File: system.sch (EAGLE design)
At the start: 36 parts, among them IC1 TPS7B8650BQDDARQ1, IC2 TLV9101IDBVR, IC3 TLV9101IDBVR, J1 TSW-104-07-F-S, J2 163-179PH-EX, U1 ATMEGA328PB-AU

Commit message: Added 0 ohm R for V_BG
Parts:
- added J3: RS1-02-G, RS1-02-G:RS1-02-G
- added R22, R23: 0, rcl:R-US_R0603
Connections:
- new net N$11: J3.2, R23.1
- net 0: now also J3.1
- net N$7: now also R22.1
- net V_BG: now also R22.2, R23.2
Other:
- note added: "AD2 Backup BG Voltage"
- note removed: "TODO: Add proper footprint for inductor R_L smol"
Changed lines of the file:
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@@
 <part name="R15" library="rcl" library_urn="urn:adsk.eagle:library:334" deviceset="R-US_" device="R0603" package3d_urn="urn:adsk.eagle:package:23555/3" value="0"/>
 <part name="R16" library="rcl" library_urn="urn:adsk.eagle:library:334" deviceset="R-US_" device="R0603" package3d_urn="urn:adsk.eagle:package:23555/3" value="0"/>
+<part name="R22" library="rcl" library_urn="urn:adsk.eagle:library:334" deviceset="R-US_" device="R0603" package3d_urn="urn:adsk.eagle:package:23555/3" value="0"/>
+<part name="J3" library="RS1-02-G" deviceset="RS1-02-G" device=""/>
+<part name="X_18" library="ngspice-simulation" library_urn="urn:adsk.eagle:library:527439" deviceset="GND" device=""/>
+<part name="R23" library="rcl" library_urn="urn:adsk.eagle:library:334" deviceset="R-US_" device="R0603" package3d_urn="urn:adsk.eagle:package:23555/3" value="0"/>
 </parts>
 <sheets>
@@
 <text x="-299.72" y="-71.12" size="1.778" layer="91">Decoupling cap</text>
 <text x="-154.94" y="-111.76" size="1.778" layer="91">Decoupling cap</text>
-<text x="-109.22" y="-127" size="1.778" layer="91">TODO:
-Add proper footprint for inductor
-R_L smol </text>
 <text x="-45.72" y="160.02" size="1.778" layer="91">Level Shifter
 Resistive divider with voltage follower
@@
 <text x="-39.37" y="-64.262" size="1.778" layer="91">Output</text>
 <text x="78.74" y="-83.82" size="1.778" layer="91">RST_ADC and V_TOGGLE from MCU</text>
+<text x="-200.66" y="30.48" size="1.778" layer="91">AD2 Backup BG Voltage</text>
 </plain>
 <moduleinsts>
@@
 <attribute name="NAME" value="LDO_AND_VOLTAGE_REFS" x="-119.38" y="63.5" size="2.032" layer="95" align="bottom-center"/>
 </moduleinst>
-<moduleinst name="BANDGAP_REF" module="BANDGAP_REF" x="-203.2" y="63.5">
-<attribute name="NAME" value="BANDGAP_REF" x="-203.2" y="63.5" size="2.032" layer="95" align="bottom-center"/>
+<moduleinst name="BANDGAP_REF" module="BANDGAP_REF" x="-210.82" y="63.5">
+<attribute name="NAME" value="BANDGAP_REF" x="-210.82" y="63.5" size="2.032" layer="95" align="bottom-center"/>
 </moduleinst>
 <moduleinst name="THERMISTOR_THERMOPILE" module="THERMISTOR_THERMOPILE" x="58.42" y="63.5">
@@
 <attribute name="VALUE" x="52.07" y="-39.878" size="1.778" layer="96" rot="R180"/>
 </instance>
+<instance part="R22" gate="G$1" x="-175.26" y="63.5" smashed="yes">
+<attribute name="NAME" x="-176.53" y="64.9986" size="1.778" layer="95"/>
+<attribute name="VALUE" x="-179.07" y="65.278" size="1.778" layer="96"/>
+</instance>
+<instance part="J3" gate="A" x="-172.72" y="40.64" smashed="yes" rot="R180">
+<attribute name="NAME" x="-179.4256" y="35.3314" size="2.0828" layer="95" ratio="6" rot="SR180"/>
+</instance>
+<instance part="X_18" gate="G$1" x="-167.64" y="35.56" smashed="yes"/>
+<instance part="R23" gate="G$1" x="-167.64" y="53.34" smashed="yes" rot="R90">
+<attribute name="NAME" x="-169.1386" y="52.07" size="1.778" layer="95" rot="R90"/>
+<attribute name="VALUE" x="-169.418" y="49.53" size="1.778" layer="96" rot="R90"/>
+</instance>
 </instances>
 <busses>
@@
 <pinref part="X_17" gate="G$1" pin="0"/>
 </segment>
+<segment>
+<pinref part="J3" gate="A" pin="1"/>
+<wire x1="-172.72" y1="40.64" x2="-167.64" y2="40.64" width="0.1524" layer="91"/>
+<wire x1="-167.64" y1="40.64" x2="-167.64" y2="35.56" width="0.1524" layer="91"/>
+<pinref part="X_18" gate="G$1" pin="0"/>
+</segment>
 </net>
 <net name="VS_9V" class="0">
@@
 <wire x1="-243.84" y1="63.5" x2="-243.84" y2="78.74" width="0.1524" layer="91"/>
 <portref moduleinst="BANDGAP_REF" port="VS_6V"/>
-<wire x1="-243.84" y1="63.5" x2="-228.6" y2="63.5" width="0.1524" layer="91"/>
+<wire x1="-243.84" y1="63.5" x2="-236.22" y2="63.5" width="0.1524" layer="91"/>
 <junction x="-243.84" y="63.5"/>
 <pinref part="R2" gate="G$1" pin="1"/>
@@
 <segment>
 <portref moduleinst="LDO_AND_VOLTAGE_REFS" port="V_BG"/>
-<portref moduleinst="BANDGAP_REF" port="V_BG"/>
-<label x="-175.26" y="63.5" size="1.778" layer="95"/>
-<wire x1="-157.48" y1="63.5" x2="-177.8" y2="63.5" width="0.1524" layer="91"/>
+<label x="-165.1" y="63.5" size="1.778" layer="95"/>
+<wire x1="-157.48" y1="63.5" x2="-167.64" y2="63.5" width="0.1524" layer="91"/>
+<pinref part="R22" gate="G$1" pin="2"/>
+<pinref part="R23" gate="G$1" pin="2"/>
+<wire x1="-167.64" y1="63.5" x2="-170.18" y2="63.5" width="0.1524" layer="91"/>
+<wire x1="-167.64" y1="58.42" x2="-167.64" y2="63.5" width="0.1524" layer="91"/>
+<junction x="-167.64" y="63.5"/>
 </segment>
 <segment>
@@
 </segment>
 </net>
+<net name="N$7" class="0">
+<segment>
+<portref moduleinst="BANDGAP_REF" port="V_BG"/>
+<pinref part="R22" gate="G$1" pin="1"/>
+<wire x1="-180.34" y1="63.5" x2="-185.42" y2="63.5" width="0.1524" layer="91"/>
+</segment>
+</net>
+<net name="N$11" class="0">
+<segment>
+<pinref part="J3" gate="A" pin="2"/>
+<wire x1="-172.72" y1="43.18" x2="-167.64" y2="43.18" width="0.1524" layer="91"/>
+<pinref part="R23" gate="G$1" pin="1"/>
+<wire x1="-167.64" y1="43.18" x2="-167.64" y2="48.26" width="0.1524" layer="91"/>
+</segment>
+</net>

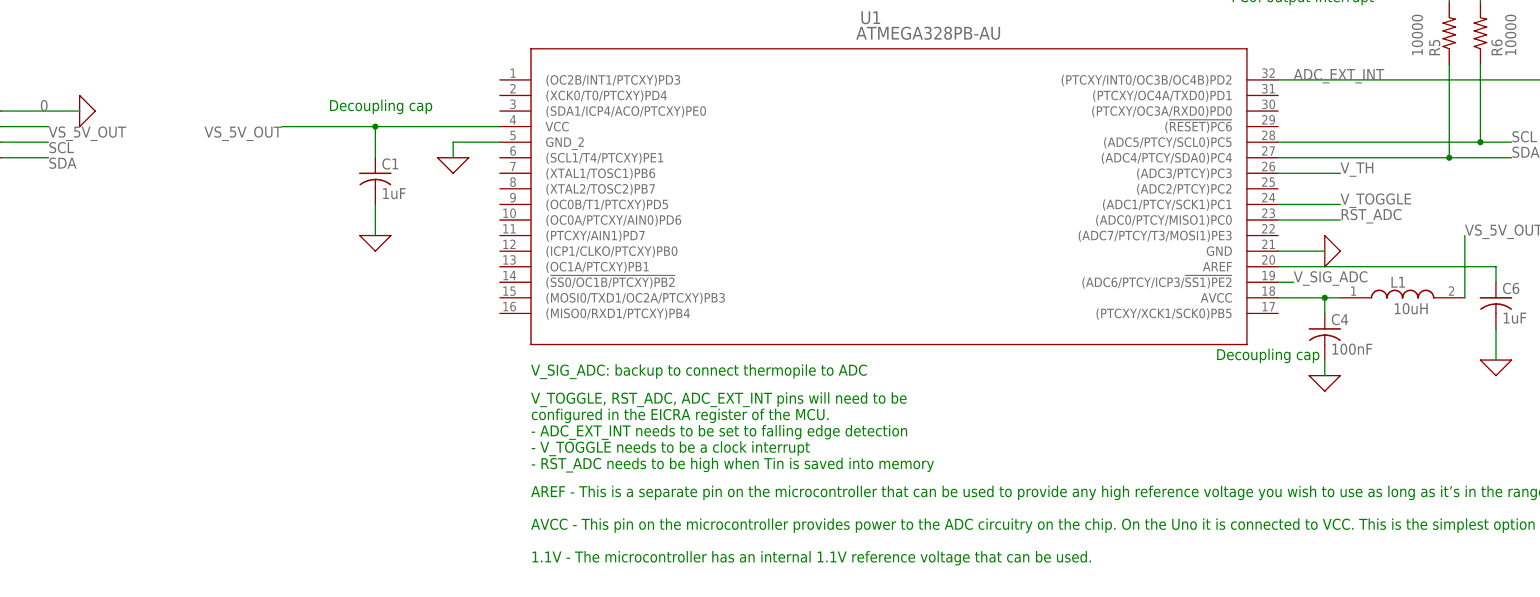
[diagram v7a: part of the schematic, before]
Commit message: push button added
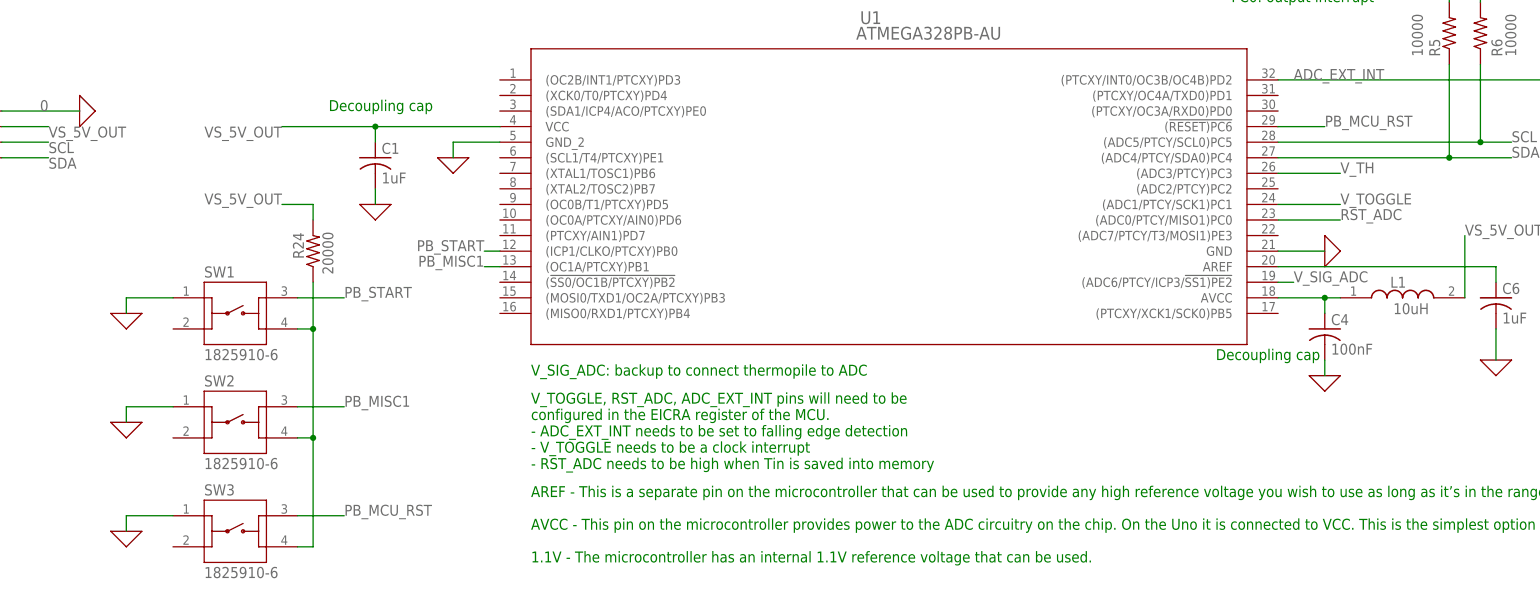
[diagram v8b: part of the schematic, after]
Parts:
- added R24: 20000, rcl:R-US_R0603
- added SW1, SW2, SW3: 1825910-6, 1825910-6:1825910-6
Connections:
- new net N$12: U1.(ICP1/CLKO/PTCXY)PB0
- new net N$13: U1.(OC1A/PTCXY)PB1
- new net N$19: R24.1, SW1.4, SW2.4, SW3.4
- new net PB_MCU_RST: SW3.3, U1.(!RESET)PC6
- new net PB_MISC1: SW2.3
- new net PB_START: SW1.3
- net 0: now also SW1.1, SW2.1, SW3.1
- net VS_5V_OUT: now also R24.2
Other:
- note removed: "TODO: add backup LDO"
- moved on the sheet: C1
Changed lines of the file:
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@@
 Outputs: VS_1.5V
 Vout = (1 + R5/R6)*Vin</text>
-<text x="-78.74" y="17.78" size="1.778" layer="91">TODO: add backup LDO</text>
 </plain>
 <instances>
@@
 <part name="X_18" library="ngspice-simulation" library_urn="urn:adsk.eagle:library:527439" deviceset="GND" device=""/>
 <part name="R23" library="rcl" library_urn="urn:adsk.eagle:library:334" deviceset="R-US_" device="R0603" package3d_urn="urn:adsk.eagle:package:23555/3" value="0"/>
+<part name="SW1" library="1825910-6" deviceset="1825910-6" device=""/>
+<part name="SW2" library="1825910-6" deviceset="1825910-6" device=""/>
+<part name="SW3" library="1825910-6" deviceset="1825910-6" device=""/>
+<part name="X_19" library="ngspice-simulation" library_urn="urn:adsk.eagle:library:527439" deviceset="GND" device=""/>
+<part name="X_20" library="ngspice-simulation" library_urn="urn:adsk.eagle:library:527439" deviceset="GND" device=""/>
+<part name="X_21" library="ngspice-simulation" library_urn="urn:adsk.eagle:library:527439" deviceset="GND" device=""/>
+<part name="R24" library="rcl" library_urn="urn:adsk.eagle:library:334" deviceset="R-US_" device="R0603" package3d_urn="urn:adsk.eagle:package:23555/3" value="20000"/>
 </parts>
 <sheets>
@@
 </instance>
 <instance part="X_3" gate="G$1" x="-279.4" y="-78.74" smashed="yes"/>
-<instance part="C1" gate="G$1" x="-292.1" y="-81.28" smashed="yes">
-<attribute name="NAME" x="-291.084" y="-80.645" size="1.778" layer="95"/>
-<attribute name="VALUE" x="-291.084" y="-85.471" size="1.778" layer="96"/>
+<instance part="C1" gate="G$1" x="-292.1" y="-78.74" smashed="yes">
+<attribute name="NAME" x="-291.084" y="-78.105" size="1.778" layer="95"/>
+<attribute name="VALUE" x="-291.084" y="-82.931" size="1.778" layer="96"/>
 </instance>
 <instance part="C4" gate="G$1" x="-137.16" y="-106.68" smashed="yes">
@@
 <attribute name="VALUE" x="-136.144" y="-110.871" size="1.778" layer="96"/>
 </instance>
-<instance part="X_5" gate="G$1" x="-292.1" y="-91.44" smashed="yes"/>
+<instance part="X_5" gate="G$1" x="-292.1" y="-86.36" smashed="yes"/>
 <instance part="X_6" gate="G$1" x="-137.16" y="-114.3" smashed="yes"/>
 <instance part="R2" gate="G$1" x="-170.18" y="78.74" smashed="yes">
@@
 <attribute name="NAME" x="-169.1386" y="52.07" size="1.778" layer="95" rot="R90"/>
 <attribute name="VALUE" x="-169.418" y="49.53" size="1.778" layer="96" rot="R90"/>
+</instance>
+<instance part="SW1" gate="G$1" x="-314.96" y="-104.14" smashed="yes">
+<attribute name="NAME" x="-320.0497" y="-98.28685" size="1.803440625" layer="95"/>
+<attribute name="VALUE" x="-320.048309375" y="-111.77246875" size="1.802940625" layer="96"/>
+</instance>
+<instance part="SW2" gate="G$1" x="-314.96" y="-121.92" smashed="yes">
+<attribute name="NAME" x="-320.0497" y="-116.06685" size="1.803440625" layer="95"/>
+<attribute name="VALUE" x="-320.048309375" y="-129.55246875" size="1.802940625" layer="96"/>
+</instance>
+<instance part="SW3" gate="G$1" x="-314.96" y="-139.7" smashed="yes">
+<attribute name="NAME" x="-320.0497" y="-133.84685" size="1.803440625" layer="95"/>
+<attribute name="VALUE" x="-320.048309375" y="-147.33246875" size="1.802940625" layer="96"/>
+</instance>
+<instance part="X_19" gate="G$1" x="-332.74" y="-121.92" smashed="yes"/>
+<instance part="X_20" gate="G$1" x="-332.74" y="-104.14" smashed="yes"/>
+<instance part="X_21" gate="G$1" x="-332.74" y="-139.7" smashed="yes"/>
+<instance part="R24" gate="G$1" x="-302.26" y="-93.98" smashed="yes" rot="R90">
+<attribute name="NAME" x="-303.7586" y="-95.25" size="1.778" layer="95" rot="R90"/>
+<attribute name="VALUE" x="-298.958" y="-97.79" size="1.778" layer="96" rot="R90"/>
 </instance>
 </instances>
@@
 <segment>
 <pinref part="C1" gate="G$1" pin="2"/>
-<wire x1="-292.1" y1="-86.36" x2="-292.1" y2="-91.44" width="0.1524" layer="91"/>
+<wire x1="-292.1" y1="-83.82" x2="-292.1" y2="-86.36" width="0.1524" layer="91"/>
 <pinref part="X_5" gate="G$1" pin="0"/>
 </segment>
@@
 <wire x1="-167.64" y1="40.64" x2="-167.64" y2="35.56" width="0.1524" layer="91"/>
 <pinref part="X_18" gate="G$1" pin="0"/>
+</segment>
+<segment>
+<pinref part="SW1" gate="G$1" pin="1"/>
+<wire x1="-325.12" y1="-101.6" x2="-332.74" y2="-101.6" width="0.1524" layer="91"/>
+<wire x1="-332.74" y1="-101.6" x2="-332.74" y2="-104.14" width="0.1524" layer="91"/>
+<pinref part="X_20" gate="G$1" pin="0"/>
+</segment>
+<segment>
+<pinref part="SW2" gate="G$1" pin="1"/>
+<wire x1="-325.12" y1="-119.38" x2="-332.74" y2="-119.38" width="0.1524" layer="91"/>
+<wire x1="-332.74" y1="-119.38" x2="-332.74" y2="-121.92" width="0.1524" layer="91"/>
+<pinref part="X_19" gate="G$1" pin="0"/>
+</segment>
+<segment>
+<pinref part="SW3" gate="G$1" pin="1"/>
+<wire x1="-325.12" y1="-137.16" x2="-332.74" y2="-137.16" width="0.1524" layer="91"/>
+<pinref part="X_21" gate="G$1" pin="0"/>
+<wire x1="-332.74" y1="-137.16" x2="-332.74" y2="-139.7" width="0.1524" layer="91"/>
 </segment>
 </net>
@@
 <pinref part="C1" gate="G$1" pin="1"/>
 <wire x1="-292.1" y1="-73.66" x2="-307.34" y2="-73.66" width="0.1524" layer="91"/>
-<wire x1="-292.1" y1="-78.74" x2="-292.1" y2="-73.66" width="0.1524" layer="91"/>
+<wire x1="-292.1" y1="-76.2" x2="-292.1" y2="-73.66" width="0.1524" layer="91"/>
 <junction x="-292.1" y="-73.66"/>
 <label x="-307.34" y="-73.66" size="1.778" layer="95" rot="R180"/>
@@
 <wire x1="53.34" y1="-53.34" x2="63.5" y2="-53.34" width="0.1524" layer="91"/>
 <label x="63.5" y="-53.34" size="1.778" layer="95"/>
+</segment>
+<segment>
+<pinref part="R24" gate="G$1" pin="2"/>
+<wire x1="-302.26" y1="-88.9" x2="-302.26" y2="-86.36" width="0.1524" layer="91"/>
+<wire x1="-302.26" y1="-86.36" x2="-307.34" y2="-86.36" width="0.1524" layer="91"/>
+<label x="-307.34" y="-86.36" size="1.778" layer="95" align="bottom-right"/>
 </segment>
 </net>
@@
 </segment>
 </net>
+<net name="N$19" class="0">
+<segment>
+<pinref part="R24" gate="G$1" pin="1"/>
+<pinref part="SW1" gate="G$1" pin="4"/>
+<wire x1="-304.8" y1="-106.68" x2="-302.26" y2="-106.68" width="0.1524" layer="91"/>
+<pinref part="SW2" gate="G$1" pin="4"/>
+<wire x1="-304.8" y1="-124.46" x2="-302.26" y2="-124.46" width="0.1524" layer="91"/>
+<wire x1="-302.26" y1="-124.46" x2="-302.26" y2="-106.68" width="0.1524" layer="91"/>
+<pinref part="SW3" gate="G$1" pin="4"/>
+<wire x1="-304.8" y1="-142.24" x2="-302.26" y2="-142.24" width="0.1524" layer="91"/>
+<wire x1="-302.26" y1="-142.24" x2="-302.26" y2="-124.46" width="0.1524" layer="91"/>
+<junction x="-302.26" y="-124.46"/>
+<wire x1="-302.26" y1="-99.06" x2="-302.26" y2="-106.68" width="0.1524" layer="91"/>
+<junction x="-302.26" y="-106.68"/>
+</segment>
+</net>
+<net name="PB_MCU_RST" class="0">
+<segment>
+<pinref part="SW3" gate="G$1" pin="3"/>
+<wire x1="-304.8" y1="-137.16" x2="-297.18" y2="-137.16" width="0.1524" layer="91"/>
+<label x="-297.18" y="-137.16" size="1.778" layer="95"/>
+</segment>
+<segment>
+<pinref part="U1" gate="A" pin="(!RESET)PC6"/>
+<wire x1="-144.78" y1="-73.66" x2="-137.16" y2="-73.66" width="0.1524" layer="91"/>
+<label x="-137.16" y="-73.66" size="1.778" layer="95"/>
+</segment>
+</net>
+<net name="PB_START" class="0">
+<segment>
+<pinref part="SW1" gate="G$1" pin="3"/>
+<wire x1="-304.8" y1="-101.6" x2="-297.18" y2="-101.6" width="0.1524" layer="91"/>
+<label x="-297.18" y="-101.6" size="1.778" layer="95"/>
+<label x="-274.32" y="-93.98" size="1.778" layer="95" align="bottom-right"/>
+</segment>
+</net>
+<net name="N$12" class="0">
+<segment>
+<pinref part="U1" gate="A" pin="(ICP1/CLKO/PTCXY)PB0"/>
+<wire x1="-271.78" y1="-93.98" x2="-274.32" y2="-93.98" width="0.1524" layer="91"/>
+</segment>
+</net>
+<net name="PB_MISC1" class="0">
+<segment>
+<pinref part="SW2" gate="G$1" pin="3"/>
+<wire x1="-304.8" y1="-119.38" x2="-297.18" y2="-119.38" width="0.1524" layer="91"/>
+<label x="-297.18" y="-119.38" size="1.778" layer="95"/>
+<label x="-274.32" y="-96.52" size="1.778" layer="95" align="bottom-right"/>
+</segment>
+</net>
+<net name="N$13" class="0">
+<segment>
+<pinref part="U1" gate="A" pin="(OC1A/PTCXY)PB1"/>
+<wire x1="-271.78" y1="-96.52" x2="-274.32" y2="-96.52" width="0.1524" layer="91"/>
+</segment>
+</net>
